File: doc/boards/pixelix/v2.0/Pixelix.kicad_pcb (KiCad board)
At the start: 2 copper layers, 100 x 50 mm, 31 parts, among them J1 Conn_01x02, J2 Conn_01x02, J3 Conn_01x03, J4 Conn_01x02, J5 Conn_02x05_Odd_Even, J6 Conn_01x02, J7 Conn_01x03, J8 Conn_01x02, Q1 NMOS_GSD_BSS138, Q2 PMOS_GDS_STD26P3LLH6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

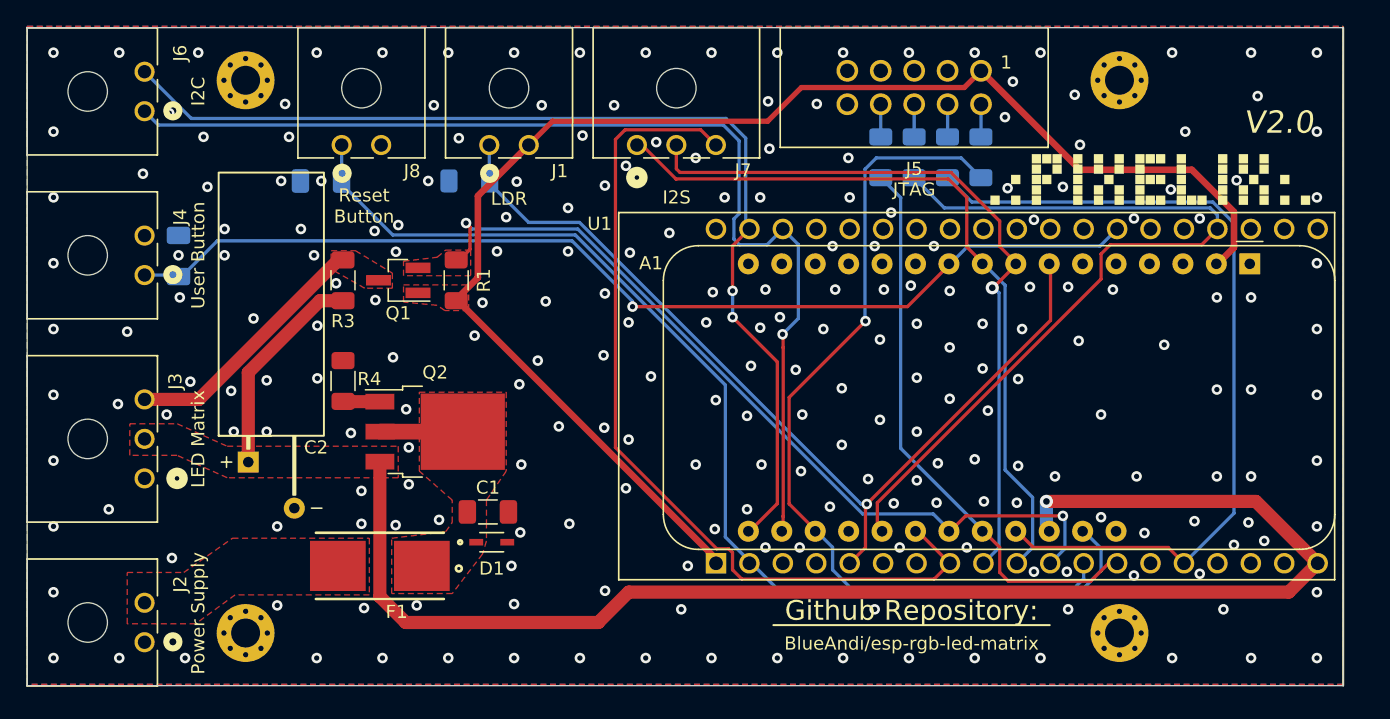
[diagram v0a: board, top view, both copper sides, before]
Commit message: Board v2.0 Schematic and PCB - DevKit: SDA from IO23 to IO21 new connected
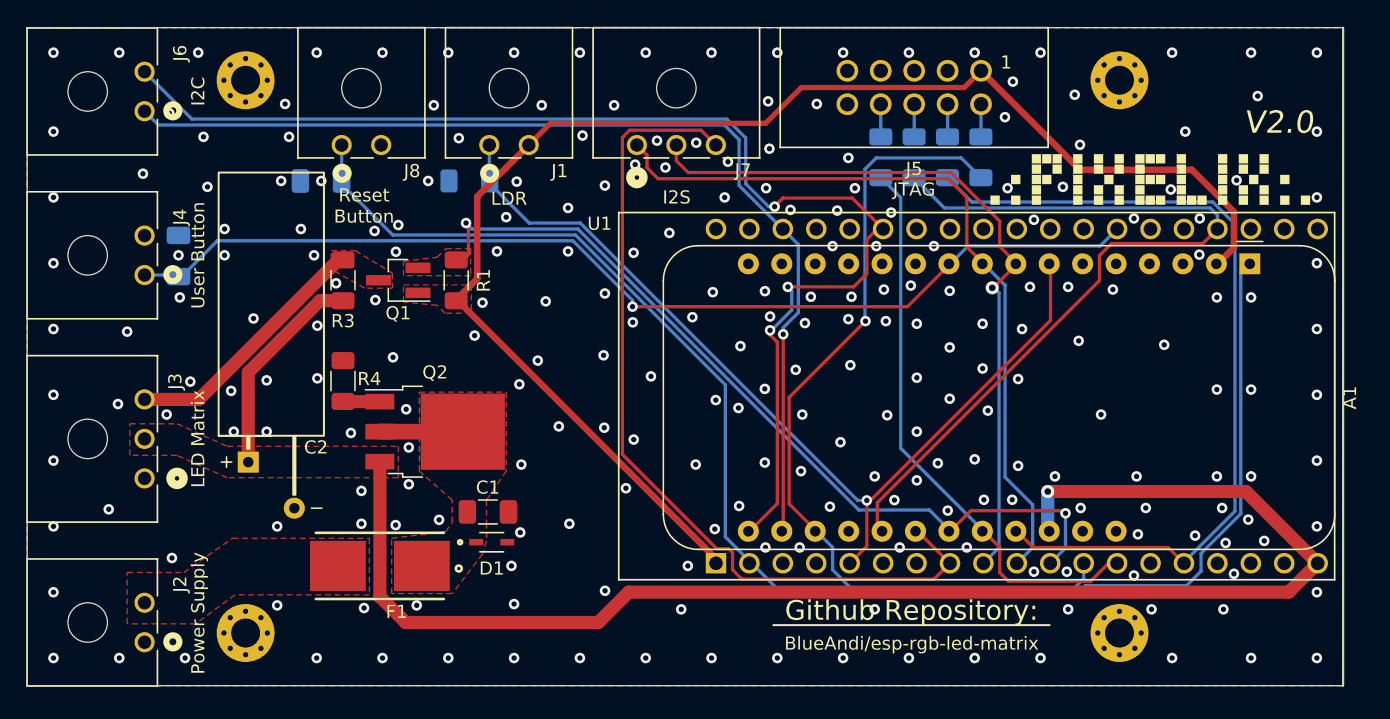
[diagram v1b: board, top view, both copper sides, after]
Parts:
- A1: value Adafruit_Feather_HUZZAH32_ESP32 -> Adafruit_Feather_V2_ESP32; footprint Module:Adafruit_Feather -> footprints:Adafruit_Feather_V2_ESP32
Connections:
- A1 pad 1: unconnected-(A1-Pad1) -> /RESET
- A1 pad 27: /RESET -> unconnected-(A1-Pad27)
- U1 pad 21: /SDA -> unconnected-(U1-Pad21)
- U1 pad 25: unconnected-(U1-Pad25) -> /SDA
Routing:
- net /RESET: track 84.7 -> 113.6 mm
- net /SDA: track 80.6 -> 94.8 mm, vias 2 -> 3
- net /SCL: track 82.1 -> 78.2 mm
- net /VCC-PROTECTED: track 125.4 -> 126.3 mm
- net /I2S_Data_IN: track 66.2 -> 65.5 mm
- net /LV-DATA-OUT: track 63.1 -> 63.8 mm
- net /I2S_CLK: track 57.1 -> 57.6 mm
- net GND: vias 234 -> 244

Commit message: Board v2.0 PCB and Gerber - small changes - create Gerber
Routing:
- net /MTCK: track 64.4 -> 66.4 mm
- net /I2S_WS: track 55.8 -> 55.0 mm
- net /MTMS: track 65.2 -> 65.8 mm
- net /SDA: track 94.8 -> 94.2 mm
- net GND: vias 244 -> 256

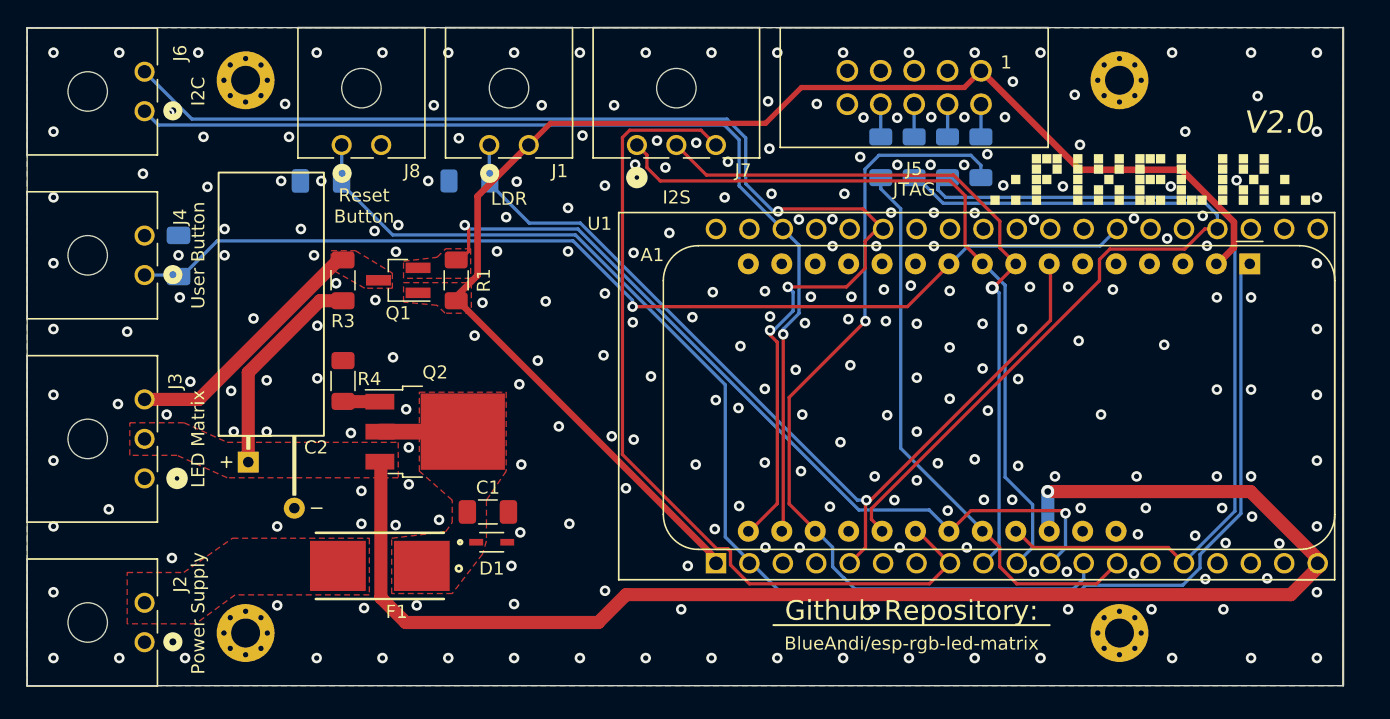
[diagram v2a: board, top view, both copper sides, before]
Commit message: Board v2.0 PCB - finished Version 2.0 with the ordering of PCBs and components
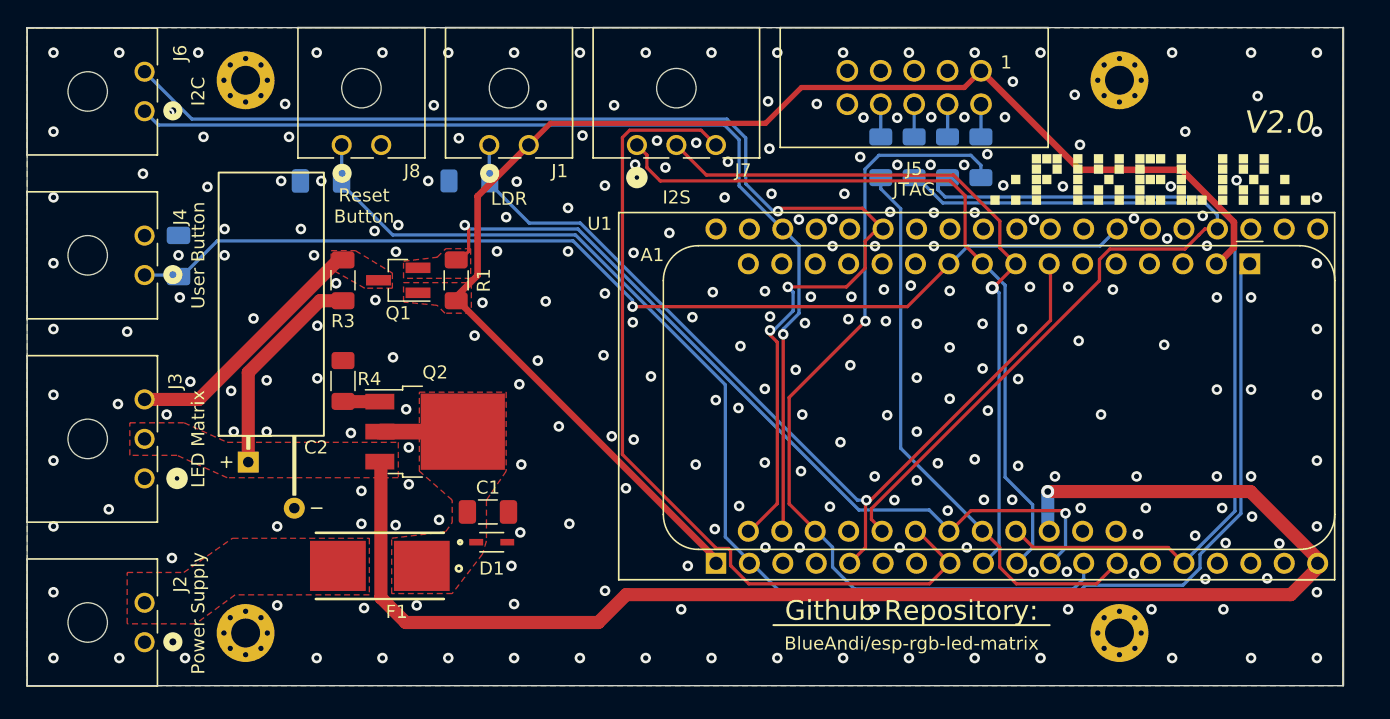
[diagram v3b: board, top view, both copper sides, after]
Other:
- rule pad_to_mask_clearance: 0 -> 0.05
- board text added: "V2.0"
- board text removed: "${REVISION}"

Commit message: Repository renamed to https://github.com/BlueAndi/Pixelix #96
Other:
- board text added: "BlueAndi/Pixelix"
- board text removed: "BlueAndi/esp-rgb-led-matrix"
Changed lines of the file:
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@@
     (effects (font (size 1 1) (thickness 0.15)))
   )
-  (gr_text "BlueAndi/esp-rgb-led-matrix " (at 168.2 116.9) (layer "F.SilkS")
+  (gr_text "BlueAndi/Pixelix " (at 168.2 116.9) (layer "F.SilkS")
     (effects (font (size 1 1) (thickness 0.15)))
   )
